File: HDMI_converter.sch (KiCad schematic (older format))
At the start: 106 parts, among them J2 46756-1001, Q1 BSS138APW, Q2 BSS138APW, Q3 BSS138APW, U2 LT9611, U3 TXB0104RUT, U4 NTS0102GT, Y2 ABM8G-24.000MHZ-18-D2Y-T

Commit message: Change LT9611_VCC12* and LT9611_VCC33* to local, change 3V3 to 3V3_sys on R59
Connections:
- net labels removed: 3V3

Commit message: Remove broken symbols of 510R resistors, add new ones
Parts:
- removed R? (x8): R_510R_0402, sa800u-baseboard-hw-footprints:0402-res, symbol sa800u-baseboard-hw:R_510R_0402
- added R? (x8): R_510R_0402, antmicro-footprints:0402-res, symbol antmicroResistors0402:R_510R_0402
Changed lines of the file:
@@
 Wire Wire Line
 	13525 7150 14300 7150
-$Comp
-L sa800u-baseboard-hw:R_510R_0402 R?
-U 1 1 62F929E9
-P 12475 6400
-F 0 "R?" V 12520 6330 60  0000 R CNN
-F 1 "R_510R_0402" H 12475 6250 60  0001 C CNN
-F 2 "sa800u-baseboard-hw-footprints:0402-res" H 12675 6600 60  0001 L CNN
-F 3 "" H 12475 6400 50  0001 C CNN
-F 4 "Yageo" H 12675 6800 60  0001 L CNN "Manufacturer"
-F 5 "RC0402JR-07510RL" H 12675 6700 60  0001 L CNN "MPN"
-F 6 "510R" V 12422 6330 50  0000 R CNN "Val"
-	1    12475 6400
-	0    -1   -1   0
-$EndComp
-$Comp
-L sa800u-baseboard-hw:R_510R_0402 R?
-U 1 1 63022A31
-P 12825 6400
-F 0 "R?" V 12870 6330 60  0000 R CNN
-F 1 "R_510R_0402" H 12825 6250 60  0001 C CNN
-F 2 "sa800u-baseboard-hw-footprints:0402-res" H 13025 6600 60  0001 L CNN
-F 3 "" H 12825 6400 50  0001 C CNN
-F 4 "Yageo" H 13025 6800 60  0001 L CNN "Manufacturer"
-F 5 "RC0402JR-07510RL" H 13025 6700 60  0001 L CNN "MPN"
-F 6 "510R" V 12772 6330 50  0000 R CNN "Val"
-	1    12825 6400
-	0    -1   -1   0
-$EndComp
-$Comp
-L sa800u-baseboard-hw:R_510R_0402 R?
-U 1 1 6306715A
-P 13175 6400
-F 0 "R?" V 13220 6330 60  0000 R CNN
-F 1 "R_510R_0402" H 13175 6250 60  0001 C CNN
-F 2 "sa800u-baseboard-hw-footprints:0402-res" H 13375 6600 60  0001 L CNN
-F 3 "" H 13175 6400 50  0001 C CNN
-F 4 "Yageo" H 13375 6800 60  0001 L CNN "Manufacturer"
-F 5 "RC0402JR-07510RL" H 13375 6700 60  0001 L CNN "MPN"
-F 6 "510R" V 13122 6330 50  0000 R CNN "Val"
-	1    13175 6400
-	0    -1   -1   0
-$EndComp
-$Comp
-L sa800u-baseboard-hw:R_510R_0402 R?
-U 1 1 630ACE68
-P 13525 6400
-F 0 "R?" V 13570 6330 60  0000 R CNN
-F 1 "R_510R_0402" H 13525 6250 60  0001 C CNN
-F 2 "sa800u-baseboard-hw-footprints:0402-res" H 13725 6600 60  0001 L CNN
-F 3 "" H 13525 6400 50  0001 C CNN
-F 4 "Yageo" H 13725 6800 60  0001 L CNN "Manufacturer"
-F 5 "RC0402JR-07510RL" H 13725 6700 60  0001 L CNN "MPN"
-F 6 "510R" V 13472 6330 50  0000 R CNN "Val"
-	1    13525 6400
-	0    -1   -1   0
-$EndComp
-$Comp
-L sa800u-baseboard-hw:R_510R_0402 R?
-U 1 1 630ACE71
-P 13875 6400
-F 0 "R?" V 13920 6330 60  0000 R CNN
-F 1 "R_510R_0402" H 13875 6250 60  0001 C CNN
-F 2 "sa800u-baseboard-hw-footprints:0402-res" H 14075 6600 60  0001 L CNN
-F 3 "" H 13875 6400 50  0001 C CNN
-F 4 "Yageo" H 14075 6800 60  0001 L CNN "Manufacturer"
-F 5 "RC0402JR-07510RL" H 14075 6700 60  0001 L CNN "MPN"
-F 6 "510R" V 13822 6330 50  0000 R CNN "Val"
-	1    13875 6400
-	0    -1   -1   0
-$EndComp
-$Comp
-L sa800u-baseboard-hw:R_510R_0402 R?
-U 1 1 630ACE7A
-P 14225 6400
-F 0 "R?" V 14270 6330 60  0000 R CNN
-F 1 "R_510R_0402" H 14225 6250 60  0001 C CNN
-F 2 "sa800u-baseboard-hw-footprints:0402-res" H 14425 6600 60  0001 L CNN
-F 3 "" H 14225 6400 50  0001 C CNN
-F 4 "Yageo" H 14425 6800 60  0001 L CNN "Manufacturer"
-F 5 "RC0402JR-07510RL" H 14425 6700 60  0001 L CNN "MPN"
-F 6 "510R" V 14172 6330 50  0000 R CNN "Val"
-	1    14225 6400
-	0    -1   -1   0
-$EndComp
-$Comp
-L sa800u-baseboard-hw:R_510R_0402 R?
-U 1 1 630F2440
-P 14575 6400
-F 0 "R?" V 14620 6330 60  0000 R CNN
-F 1 "R_510R_0402" H 14575 6250 60  0001 C CNN
-F 2 "sa800u-baseboard-hw-footprints:0402-res" H 14775 6600 60  0001 L CNN
-F 3 "" H 14575 6400 50  0001 C CNN
-F 4 "Yageo" H 14775 6800 60  0001 L CNN "Manufacturer"
-F 5 "RC0402JR-07510RL" H 14775 6700 60  0001 L CNN "MPN"
-F 6 "510R" V 14522 6330 50  0000 R CNN "Val"
-	1    14575 6400
-	0    -1   -1   0
-$EndComp
-$Comp
-L sa800u-baseboard-hw:R_510R_0402 R?
-U 1 1 630F2449
-P 14925 6400
-F 0 "R?" V 14970 6330 60  0000 R CNN
-F 1 "R_510R_0402" H 14925 6250 60  0001 C CNN
-F 2 "sa800u-baseboard-hw-footprints:0402-res" H 15125 6600 60  0001 L CNN
-F 3 "" H 14925 6400 50  0001 C CNN
-F 4 "Yageo" H 15125 6800 60  0001 L CNN "Manufacturer"
-F 5 "RC0402JR-07510RL" H 15125 6700 60  0001 L CNN "MPN"
-F 6 "510R" V 14872 6330 50  0000 R CNN "Val"
-	1    14925 6400
-	0    -1   -1   0
-$EndComp
 Text Label 2725 900  2    50   ~ 0
 LT9611_VCC33_IO
@@
 Wire Wire Line
 	4800 4925 5625 4925
+$Comp
+L antmicroResistors0402:R_510R_0402 R?
+U 1 1 62E016CC
+P 12475 6400
+F 0 "R?" V 12430 6470 60  0000 L CNN
+F 1 "R_510R_0402" H 12475 6250 60  0001 C CNN
+F 2 "antmicro-footprints:0402-res" H 12675 6600 60  0001 L CNN
+F 3 "" H 12475 6400 50  0001 C CNN
+F 4 "Yageo" H 12675 6800 60  0001 L CNN "Manufacturer"
+F 5 "RC0402JR-07510RL" H 12675 6700 60  0001 L CNN "MPN"
+F 6 "510R" V 12528 6470 50  0000 L CNN "Val"
+	1    12475 6400
+	0    1    1    0
+$EndComp
+$Comp
+L antmicroResistors0402:R_510R_0402 R?
+U 1 1 62E4D5ED
+P 12825 6400
+F 0 "R?" V 12780 6470 60  0000 L CNN
+F 1 "R_510R_0402" H 12825 6250 60  0001 C CNN
+F 2 "antmicro-footprints:0402-res" H 13025 6600 60  0001 L CNN
+F 3 "" H 12825 6400 50  0001 C CNN
+F 4 "Yageo" H 13025 6800 60  0001 L CNN "Manufacturer"
+F 5 "RC0402JR-07510RL" H 13025 6700 60  0001 L CNN "MPN"
+F 6 "510R" V 12878 6470 50  0000 L CNN "Val"
+	1    12825 6400
+	0    1    1    0
+$EndComp
+$Comp
+L antmicroResistors0402:R_510R_0402 R?
+U 1 1 62E92C49
+P 13175 6400
+F 0 "R?" V 13130 6470 60  0000 L CNN
+F 1 "R_510R_0402" H 13175 6250 60  0001 C CNN
+F 2 "antmicro-footprints:0402-res" H 13375 6600 60  0001 L CNN
+F 3 "" H 13175 6400 50  0001 C CNN
+F 4 "Yageo" H 13375 6800 60  0001 L CNN "Manufacturer"
+F 5 "RC0402JR-07510RL" H 13375 6700 60  0001 L CNN "MPN"
+F 6 "510R" V 13228 6470 50  0000 L CNN "Val"
+	1    13175 6400
+	0    1    1    0
+$EndComp
+$Comp
+L antmicroResistors0402:R_510R_0402 R?
+U 1 1 62E92C52
+P 13525 6400
+F 0 "R?" V 13480 6470 60  0000 L CNN
+F 1 "R_510R_0402" H 13525 6250 60  0001 C CNN
+F 2 "antmicro-footprints:0402-res" H 13725 6600 60  0001 L CNN
+F 3 "" H 13525 6400 50  0001 C CNN
+F 4 "Yageo" H 13725 6800 60  0001 L CNN "Manufacturer"
+F 5 "RC0402JR-07510RL" H 13725 6700 60  0001 L CNN "MPN"
+F 6 "510R" V 13578 6470 50  0000 L CNN "Val"
+	1    13525 6400
+	0    1    1    0
+$EndComp
+$Comp
+L antmicroResistors0402:R_510R_0402 R?
+U 1 1 62ED7826
+P 13875 6400
+F 0 "R?" V 13830 6470 60  0000 L CNN
+F 1 "R_510R_0402" H 13875 6250 60  0001 C CNN
+F 2 "antmicro-footprints:0402-res" H 14075 6600 60  0001 L CNN
+F 3 "" H 13875 6400 50  0001 C CNN
+F 4 "Yageo" H 14075 6800 60  0001 L CNN "Manufacturer"
+F 5 "RC0402JR-07510RL" H 14075 6700 60  0001 L CNN "MPN"
+F 6 "510R" V 13928 6470 50  0000 L CNN "Val"
+	1    13875 6400
+	0    1    1    0
+$EndComp
+$Comp
+L antmicroResistors0402:R_510R_0402 R?
+U 1 1 62ED782F
+P 14225 6400
+F 0 "R?" V 14180 6470 60  0000 L CNN
+F 1 "R_510R_0402" H 14225 6250 60  0001 C CNN
+F 2 "antmicro-footprints:0402-res" H 14425 6600 60  0001 L CNN
+F 3 "" H 14225 6400 50  0001 C CNN
+F 4 "Yageo" H 14425 6800 60  0001 L CNN "Manufacturer"
+F 5 "RC0402JR-07510RL" H 14425 6700 60  0001 L CNN "MPN"
+F 6 "510R" V 14278 6470 50  0000 L CNN "Val"
+	1    14225 6400
+	0    1    1    0
+$EndComp
+$Comp
+L antmicroResistors0402:R_510R_0402 R?
+U 1 1 62F1C359
+P 14575 6400
+F 0 "R?" V 14530 6470 60  0000 L CNN
+F 1 "R_510R_0402" H 14575 6250 60  0001 C CNN
+F 2 "antmicro-footprints:0402-res" H 14775 6600 60  0001 L CNN
+F 3 "" H 14575 6400 50  0001 C CNN
+F 4 "Yageo" H 14775 6800 60  0001 L CNN "Manufacturer"
+F 5 "RC0402JR-07510RL" H 14775 6700 60  0001 L CNN "MPN"
+F 6 "510R" V 14628 6470 50  0000 L CNN "Val"
+	1    14575 6400
+	0    1    1    0
+$EndComp
+$Comp
+L antmicroResistors0402:R_510R_0402 R?
+U 1 1 62F1C362
+P 14925 6400
+F 0 "R?" V 14880 6470 60  0000 L CNN
+F 1 "R_510R_0402" H 14925 6250 60  0001 C CNN
+F 2 "antmicro-footprints:0402-res" H 15125 6600 60  0001 L CNN
+F 3 "" H 14925 6400 50  0001 C CNN
+F 4 "Yageo" H 15125 6800 60  0001 L CNN "Manufacturer"
+F 5 "RC0402JR-07510RL" H 15125 6700 60  0001 L CNN "MPN"
+F 6 "510R" V 14978 6470 50  0000 L CNN "Val"
+	1    14925 6400
+	0    1    1    0
+$EndComp
 $EndSCHEMATC

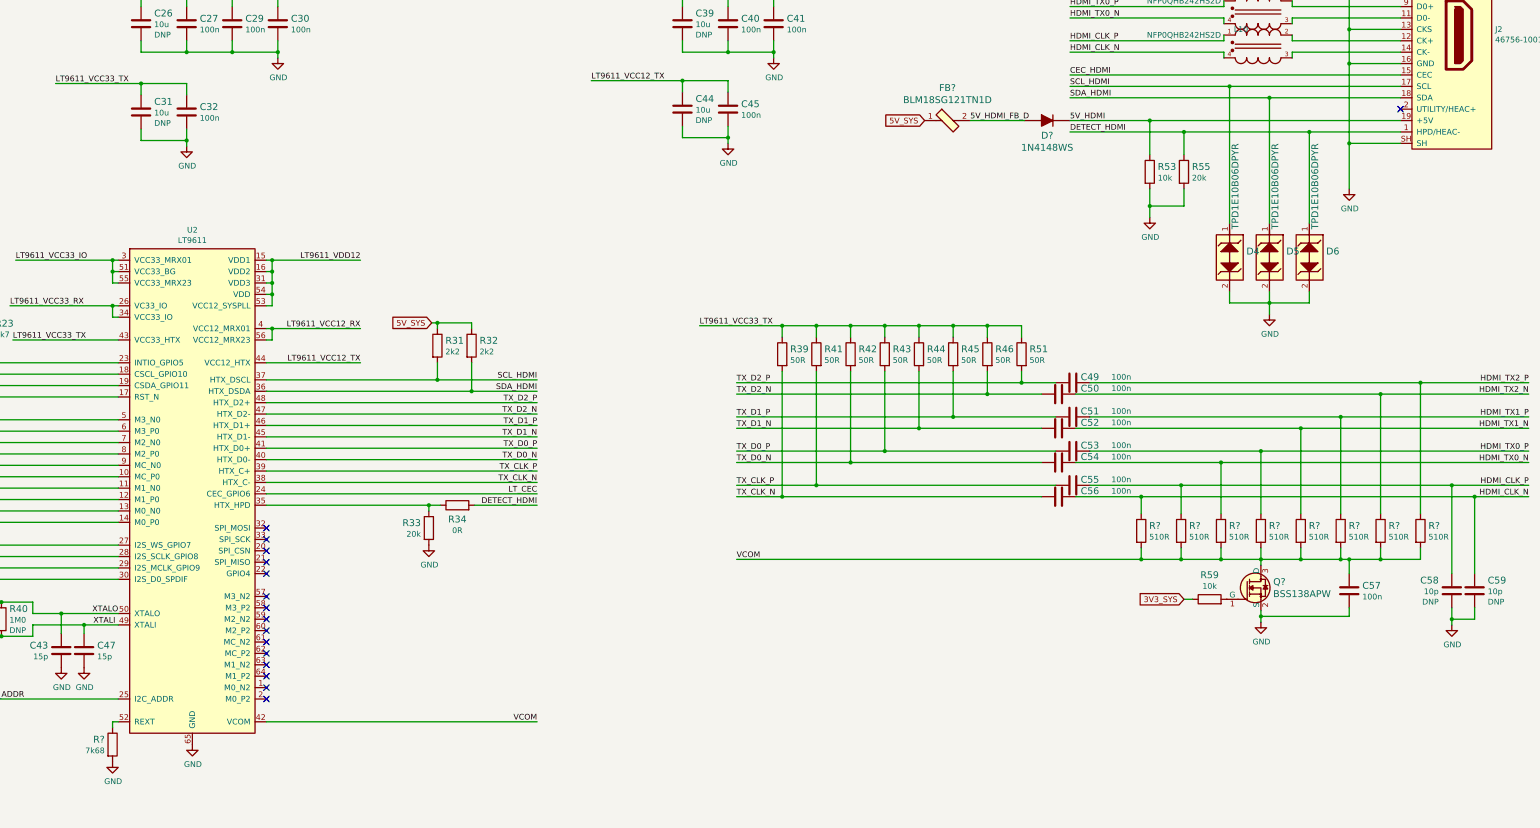
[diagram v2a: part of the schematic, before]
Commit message: Annotate parts
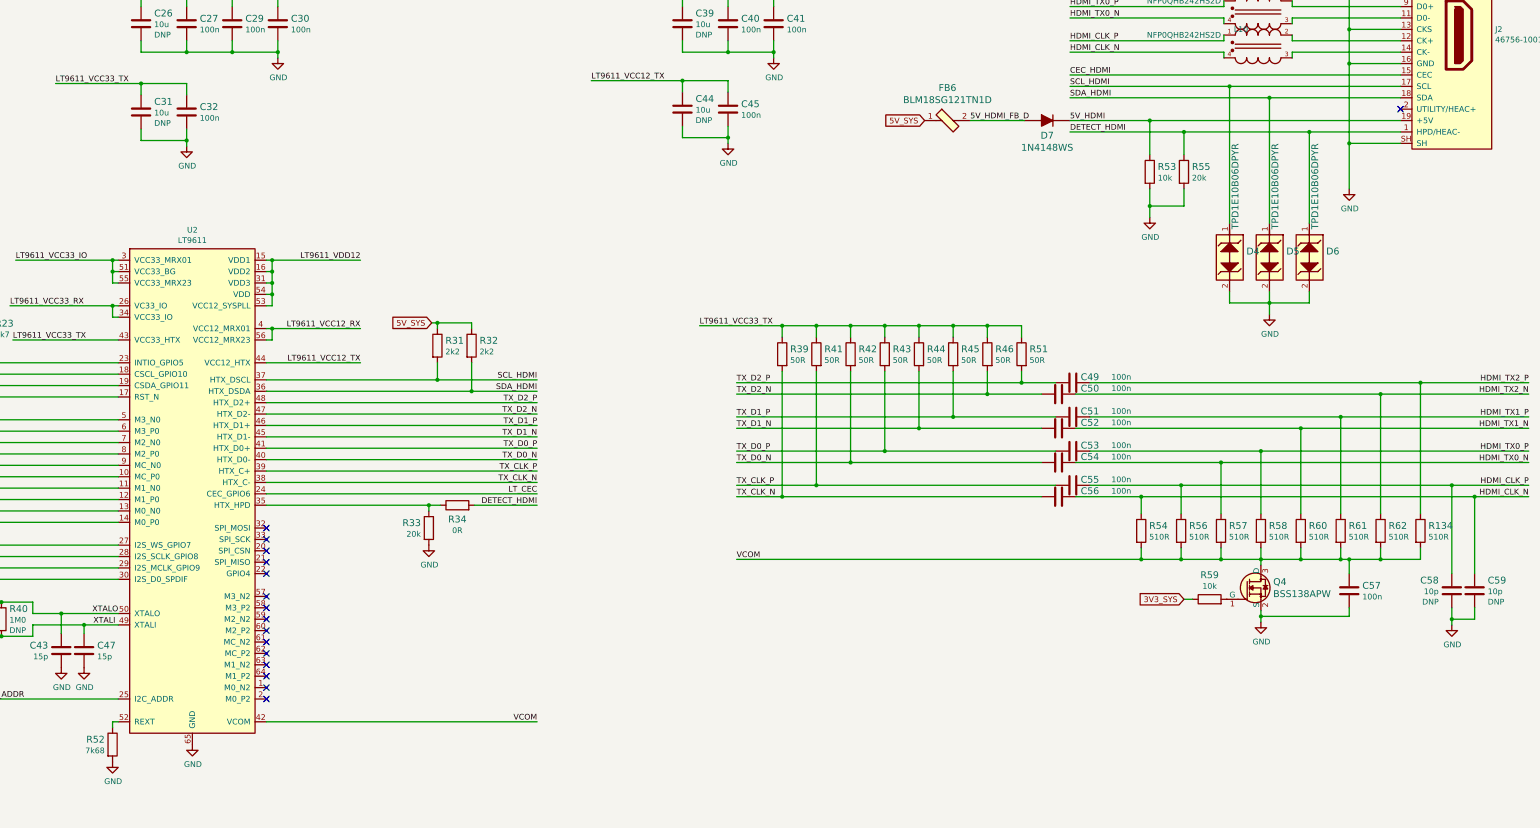
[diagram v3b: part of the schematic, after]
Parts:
- gave numbers to parts that had none: 12
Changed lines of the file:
@@
 VREG_S4A_1V8
 $Comp
-L sa800u-baseboard-hw:R_7k68_0603 R?
+L sa800u-baseboard-hw:R_7k68_0603 R52
 U 1 1 626DBF4F
 P 3450 8275
-F 0 "R?" V 3405 8206 60  0000 R CNN
+F 0 "R52" V 3405 8206 60  0000 R CNN
 F 1 "R_7k68_0603" H 3450 8125 60  0001 C CNN
 F 2 "sa800u-baseboard-hw-footprints:0603-res" H 3650 8475 60  0001 L CNN
@@
 $EndComp
 $Comp
-L sa800u-baseboard-hw:BLM18SG121TN1D FB?
+L sa800u-baseboard-hw:BLM18SG121TN1D FB6
 U 1 1 627F8CBD
 P 10775 2800
-F 0 "FB?" H 10775 3087 60  0000 C CNN
+F 0 "FB6" H 10775 3087 60  0000 C CNN
 F 1 "BLM18SG121TN1D" H 10775 2981 60  0000 C CNN
 F 2 "sa800u-baseboard-hw-footprints:0603-res" H 10975 3000 60  0001 L CNN
@@
 5V_HDMI_FB_D
 $Comp
-L sa800u-baseboard-hw:1N4148WS D?
+L sa800u-baseboard-hw:1N4148WS D7
 U 1 1 62850ADD
 P 11650 2800
-F 0 "D?" H 11650 2669 60  0000 C CNN
+F 0 "D7" H 11650 2669 60  0000 C CNN
 F 1 "1N4148WS" H 11650 2563 60  0000 C CNN
 F 2 "sa800u-baseboard-hw-footprints:SOD-323F" H 11850 3000 60  0001 L CNN
@@
 	14300 2300 14300 3000
 $Comp
-L sa800u-baseboard-hw:BSS138APW Q?
+L sa800u-baseboard-hw:BSS138APW Q4
 U 1 1 62DCD436
 P 13525 6900
-F 0 "Q?" H 13633 6953 60  0000 L CNN
+F 0 "Q4" H 13633 6953 60  0000 L CNN
 F 1 "BSS138APW" H 13633 6847 60  0000 L CNN
 F 2 "sa800u-baseboard-hw-footprints:SC70-3" H 13725 7100 60  0001 L CNN
@@
 	4800 4925 5625 4925
 $Comp
-L antmicroResistors0402:R_510R_0402 R?
+L antmicroResistors0402:R_510R_0402 R54
 U 1 1 62E016CC
 P 12475 6400
-F 0 "R?" V 12430 6470 60  0000 L CNN
+F 0 "R54" V 12430 6470 60  0000 L CNN
 F 1 "R_510R_0402" H 12475 6250 60  0001 C CNN
 F 2 "antmicro-footprints:0402-res" H 12675 6600 60  0001 L CNN
@@
 $EndComp
 $Comp
-L antmicroResistors0402:R_510R_0402 R?
+L antmicroResistors0402:R_510R_0402 R56
 U 1 1 62E4D5ED
 P 12825 6400
-F 0 "R?" V 12780 6470 60  0000 L CNN
+F 0 "R56" V 12780 6470 60  0000 L CNN
 F 1 "R_510R_0402" H 12825 6250 60  0001 C CNN
 F 2 "antmicro-footprints:0402-res" H 13025 6600 60  0001 L CNN
@@
 $EndComp
 $Comp
-L antmicroResistors0402:R_510R_0402 R?
+L antmicroResistors0402:R_510R_0402 R57
 U 1 1 62E92C49
 P 13175 6400
-F 0 "R?" V 13130 6470 60  0000 L CNN
+F 0 "R57" V 13130 6470 60  0000 L CNN
 F 1 "R_510R_0402" H 13175 6250 60  0001 C CNN
 F 2 "antmicro-footprints:0402-res" H 13375 6600 60  0001 L CNN
@@
 $EndComp
 $Comp
-L antmicroResistors0402:R_510R_0402 R?
+L antmicroResistors0402:R_510R_0402 R58
 U 1 1 62E92C52
 P 13525 6400
-F 0 "R?" V 13480 6470 60  0000 L CNN
+F 0 "R58" V 13480 6470 60  0000 L CNN
 F 1 "R_510R_0402" H 13525 6250 60  0001 C CNN
 F 2 "antmicro-footprints:0402-res" H 13725 6600 60  0001 L CNN
@@
 $EndComp
 $Comp
-L antmicroResistors0402:R_510R_0402 R?
+L antmicroResistors0402:R_510R_0402 R60
 U 1 1 62ED7826
 P 13875 6400
-F 0 "R?" V 13830 6470 60  0000 L CNN
+F 0 "R60" V 13830 6470 60  0000 L CNN
 F 1 "R_510R_0402" H 13875 6250 60  0001 C CNN
 F 2 "antmicro-footprints:0402-res" H 14075 6600 60  0001 L CNN
@@
 $EndComp
 $Comp
-L antmicroResistors0402:R_510R_0402 R?
+L antmicroResistors0402:R_510R_0402 R61
 U 1 1 62ED782F
 P 14225 6400
-F 0 "R?" V 14180 6470 60  0000 L CNN
+F 0 "R61" V 14180 6470 60  0000 L CNN
 F 1 "R_510R_0402" H 14225 6250 60  0001 C CNN
 F 2 "antmicro-footprints:0402-res" H 14425 6600 60  0001 L CNN
@@
 $EndComp
 $Comp
-L antmicroResistors0402:R_510R_0402 R?
+L antmicroResistors0402:R_510R_0402 R62
 U 1 1 62F1C359
 P 14575 6400
-F 0 "R?" V 14530 6470 60  0000 L CNN
+F 0 "R62" V 14530 6470 60  0000 L CNN
 F 1 "R_510R_0402" H 14575 6250 60  0001 C CNN
 F 2 "antmicro-footprints:0402-res" H 14775 6600 60  0001 L CNN
@@
 $EndComp
 $Comp
-L antmicroResistors0402:R_510R_0402 R?
+L antmicroResistors0402:R_510R_0402 R134
 U 1 1 62F1C362
 P 14925 6400
-F 0 "R?" V 14880 6470 60  0000 L CNN
+F 0 "R134" V 14880 6470 60  0000 L CNN
 F 1 "R_510R_0402" H 14925 6250 60  0001 C CNN
 F 2 "antmicro-footprints:0402-res" H 15125 6600 60  0001 L CNN

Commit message: Loclib
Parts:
- R134, R54, R56, R57, R58, R60, R61, R62: footprint antmicro-footprints:0402-res -> sa800u-baseboard-hw-footprints:0402-res; symbol antmicroResistors0402:R_510R_0402 -> sa800u-baseboard-hw:R_510R_0402
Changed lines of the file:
@@
 	4800 4925 5625 4925
 $Comp
-L antmicroResistors0402:R_510R_0402 R54
+L sa800u-baseboard-hw:R_510R_0402 R54
 U 1 1 62E016CC
 P 12475 6400
 F 0 "R54" V 12430 6470 60  0000 L CNN
 F 1 "R_510R_0402" H 12475 6250 60  0001 C CNN
-F 2 "antmicro-footprints:0402-res" H 12675 6600 60  0001 L CNN
+F 2 "sa800u-baseboard-hw-footprints:0402-res" H 12675 6600 60  0001 L CNN
 F 3 "" H 12475 6400 50  0001 C CNN
 F 4 "Yageo" H 12675 6800 60  0001 L CNN "Manufacturer"
@@
 $EndComp
 $Comp
-L antmicroResistors0402:R_510R_0402 R56
+L sa800u-baseboard-hw:R_510R_0402 R56
 U 1 1 62E4D5ED
 P 12825 6400
 F 0 "R56" V 12780 6470 60  0000 L CNN
 F 1 "R_510R_0402" H 12825 6250 60  0001 C CNN
-F 2 "antmicro-footprints:0402-res" H 13025 6600 60  0001 L CNN
+F 2 "sa800u-baseboard-hw-footprints:0402-res" H 13025 6600 60  0001 L CNN
 F 3 "" H 12825 6400 50  0001 C CNN
 F 4 "Yageo" H 13025 6800 60  0001 L CNN "Manufacturer"
@@
 $EndComp
 $Comp
-L antmicroResistors0402:R_510R_0402 R57
+L sa800u-baseboard-hw:R_510R_0402 R57
 U 1 1 62E92C49
 P 13175 6400
 F 0 "R57" V 13130 6470 60  0000 L CNN
 F 1 "R_510R_0402" H 13175 6250 60  0001 C CNN
-F 2 "antmicro-footprints:0402-res" H 13375 6600 60  0001 L CNN
+F 2 "sa800u-baseboard-hw-footprints:0402-res" H 13375 6600 60  0001 L CNN
 F 3 "" H 13175 6400 50  0001 C CNN
 F 4 "Yageo" H 13375 6800 60  0001 L CNN "Manufacturer"
@@
 $EndComp
 $Comp
-L antmicroResistors0402:R_510R_0402 R58
+L sa800u-baseboard-hw:R_510R_0402 R58
 U 1 1 62E92C52
 P 13525 6400
 F 0 "R58" V 13480 6470 60  0000 L CNN
 F 1 "R_510R_0402" H 13525 6250 60  0001 C CNN
-F 2 "antmicro-footprints:0402-res" H 13725 6600 60  0001 L CNN
+F 2 "sa800u-baseboard-hw-footprints:0402-res" H 13725 6600 60  0001 L CNN
 F 3 "" H 13525 6400 50  0001 C CNN
 F 4 "Yageo" H 13725 6800 60  0001 L CNN "Manufacturer"
@@
 $EndComp
 $Comp
-L antmicroResistors0402:R_510R_0402 R60
+L sa800u-baseboard-hw:R_510R_0402 R60
 U 1 1 62ED7826
 P 13875 6400
 F 0 "R60" V 13830 6470 60  0000 L CNN
 F 1 "R_510R_0402" H 13875 6250 60  0001 C CNN
-F 2 "antmicro-footprints:0402-res" H 14075 6600 60  0001 L CNN
+F 2 "sa800u-baseboard-hw-footprints:0402-res" H 14075 6600 60  0001 L CNN
 F 3 "" H 13875 6400 50  0001 C CNN
 F 4 "Yageo" H 14075 6800 60  0001 L CNN "Manufacturer"
@@
 $EndComp
 $Comp
-L antmicroResistors0402:R_510R_0402 R61
+L sa800u-baseboard-hw:R_510R_0402 R61
 U 1 1 62ED782F
 P 14225 6400
 F 0 "R61" V 14180 6470 60  0000 L CNN
 F 1 "R_510R_0402" H 14225 6250 60  0001 C CNN
-F 2 "antmicro-footprints:0402-res" H 14425 6600 60  0001 L CNN
+F 2 "sa800u-baseboard-hw-footprints:0402-res" H 14425 6600 60  0001 L CNN
 F 3 "" H 14225 6400 50  0001 C CNN
 F 4 "Yageo" H 14425 6800 60  0001 L CNN "Manufacturer"
@@
 $EndComp
 $Comp
-L antmicroResistors0402:R_510R_0402 R62
+L sa800u-baseboard-hw:R_510R_0402 R62
 U 1 1 62F1C359
 P 14575 6400
 F 0 "R62" V 14530 6470 60  0000 L CNN
 F 1 "R_510R_0402" H 14575 6250 60  0001 C CNN
-F 2 "antmicro-footprints:0402-res" H 14775 6600 60  0001 L CNN
+F 2 "sa800u-baseboard-hw-footprints:0402-res" H 14775 6600 60  0001 L CNN
 F 3 "" H 14575 6400 50  0001 C CNN
 F 4 "Yageo" H 14775 6800 60  0001 L CNN "Manufacturer"
@@
 $EndComp
 $Comp
-L antmicroResistors0402:R_510R_0402 R134
+L sa800u-baseboard-hw:R_510R_0402 R134
 U 1 1 62F1C362
 P 14925 6400
 F 0 "R134" V 14880 6470 60  0000 L CNN
 F 1 "R_510R_0402" H 14925 6250 60  0001 C CNN
-F 2 "antmicro-footprints:0402-res" H 15125 6600 60  0001 L CNN
+F 2 "sa800u-baseboard-hw-footprints:0402-res" H 15125 6600 60  0001 L CNN
 F 3 "" H 14925 6400 50  0001 C CNN
 F 4 "Yageo" H 15125 6800 60  0001 L CNN "Manufacturer"

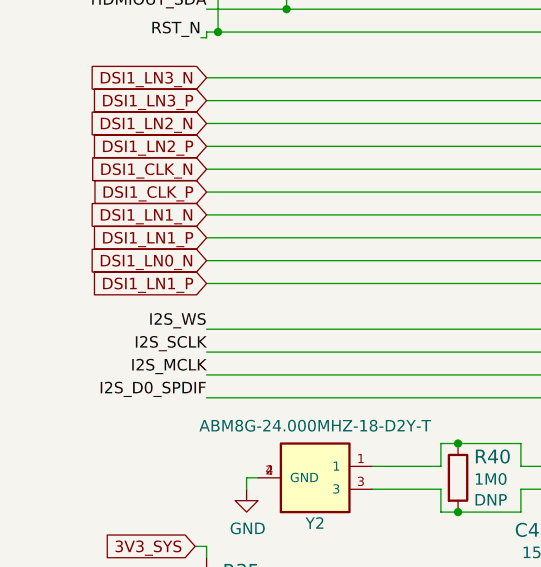
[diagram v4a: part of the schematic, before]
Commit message: Fix typo in label
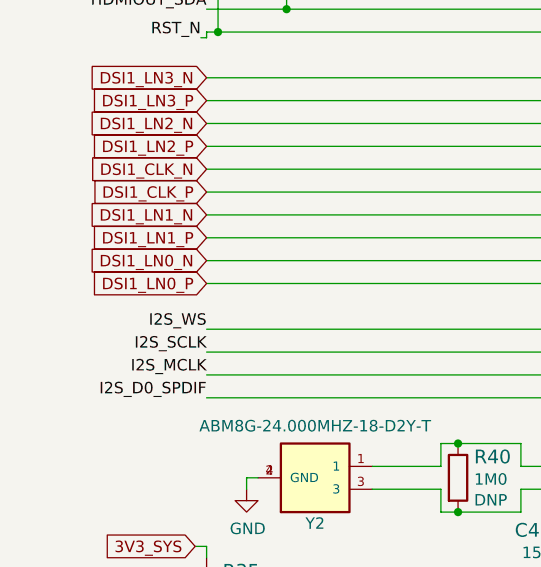
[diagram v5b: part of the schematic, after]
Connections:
- net labels added: DSI1_LN0_P
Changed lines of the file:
@@
 Text GLabel 1375 6225 0    50   Input ~ 0
 DSI1_LN0_N
-Text GLabel 1375 6325 0    50   Input ~ 0
-DSI1_LN1_P
 $Comp
 L sa800u-baseboard-hw:46756-1001 J2
@@
 	0    1    1    0
 $EndComp
+Text GLabel 1375 6325 0    50   Input ~ 0
+DSI1_LN0_P
 $EndSCHEMATC
